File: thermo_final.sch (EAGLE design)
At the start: 109 parts

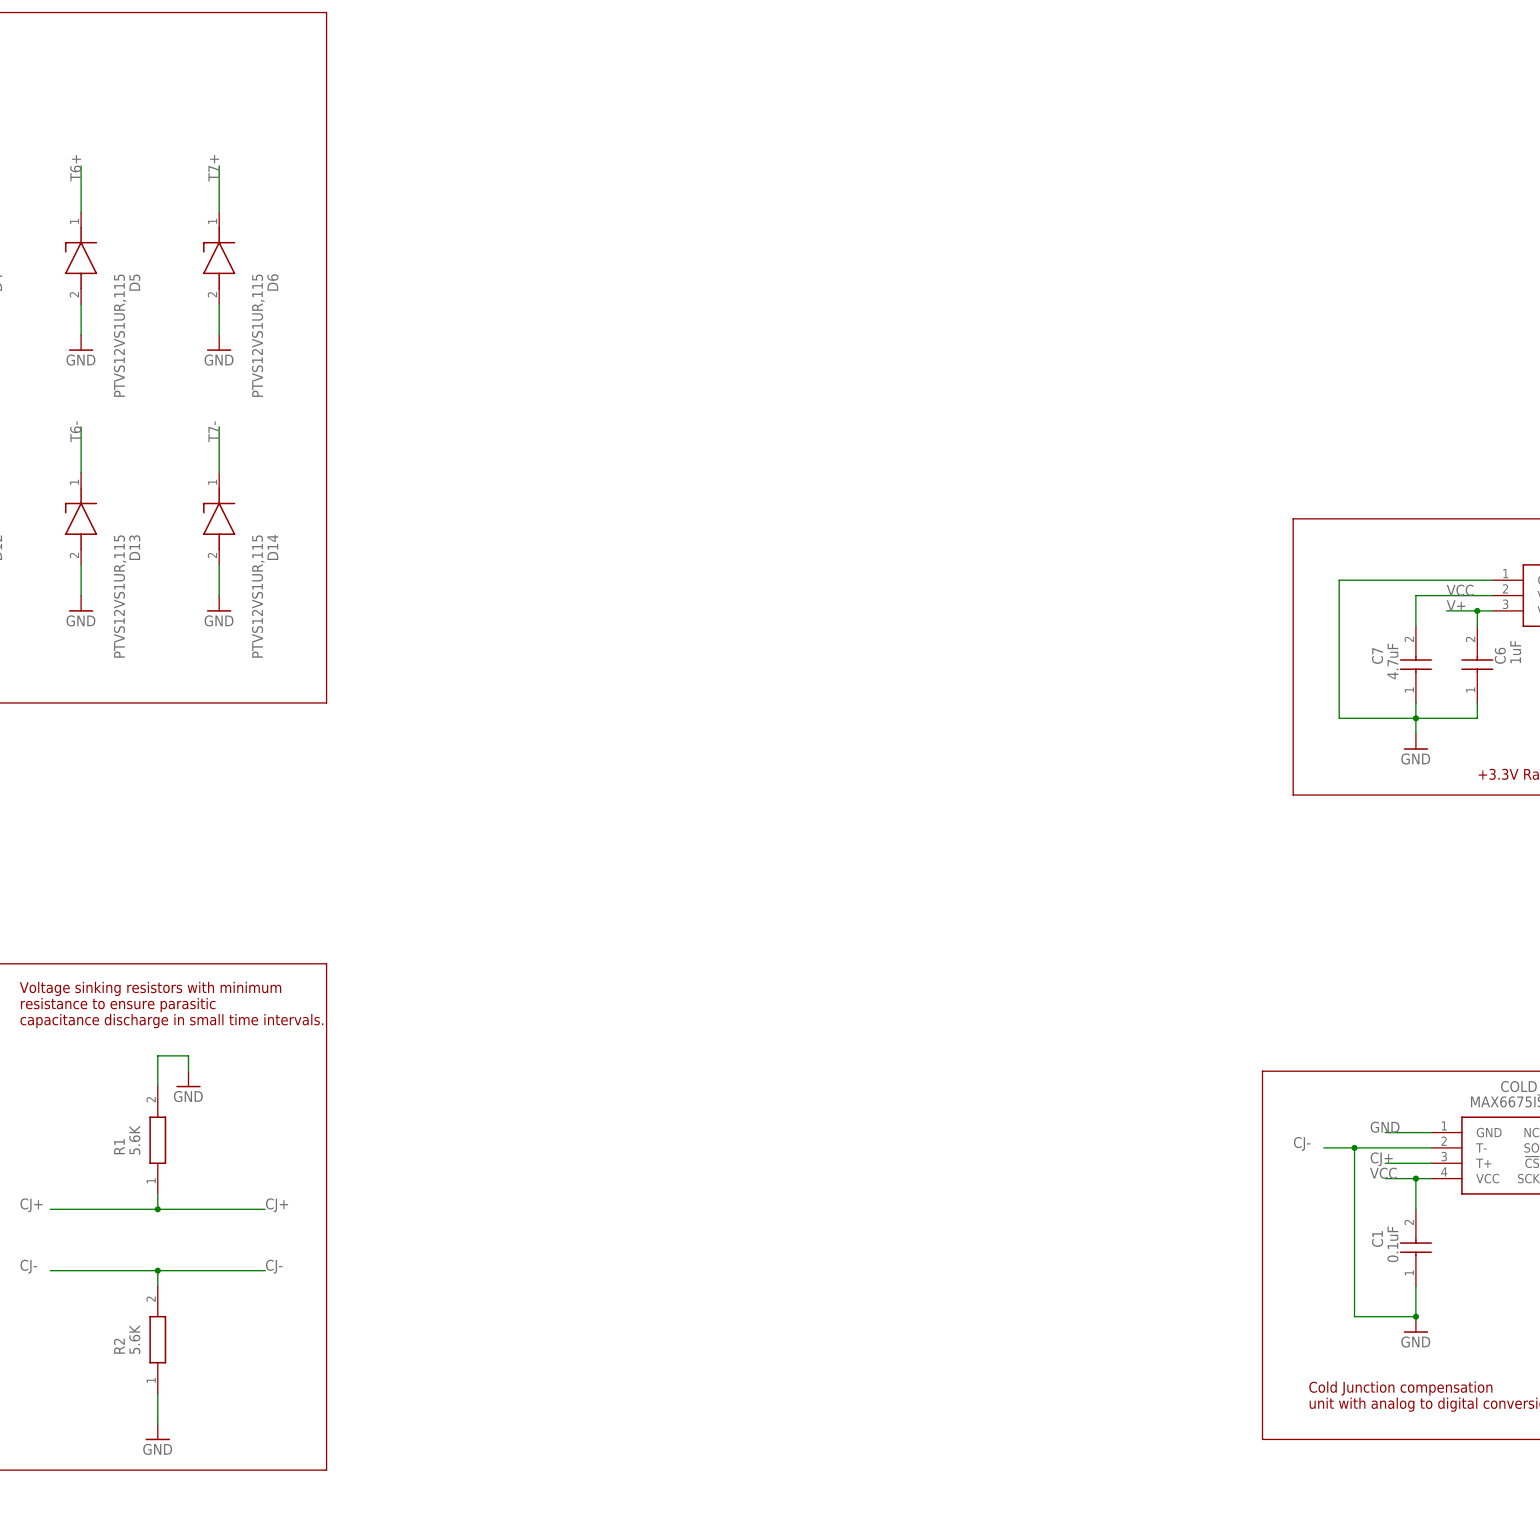
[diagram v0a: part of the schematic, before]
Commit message: Final w/GND vias & Enclosure Holes
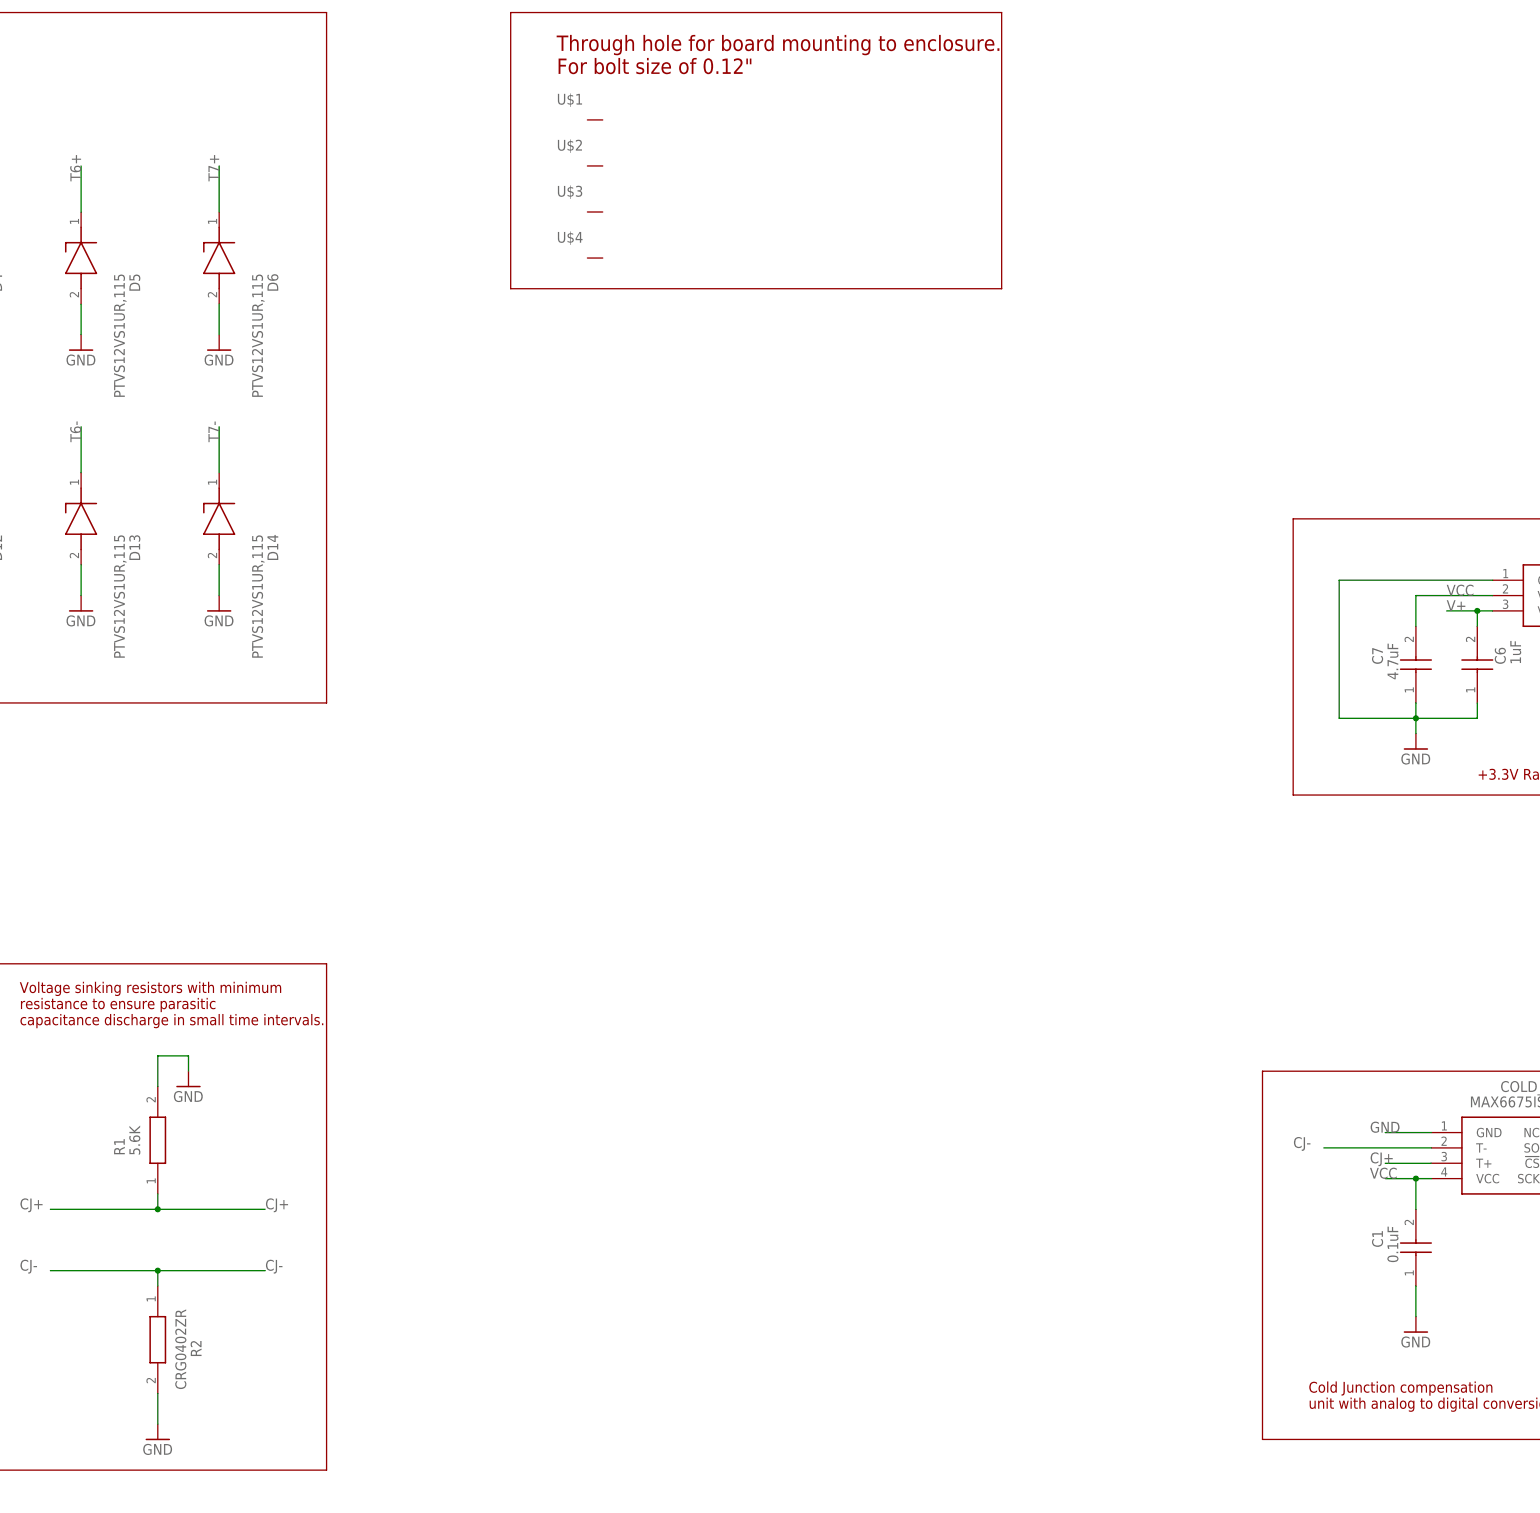
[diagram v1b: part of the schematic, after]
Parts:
- added U$1, U$2, U$3, U$4: THROUGH_HOLE, SamacSys_Parts:THROUGH_HOLE
- R2: value 5.6K -> CRG0402ZR; device SamacSys_Parts:ERA-2ARB562X -> SamacSys_Parts:CRG0402ZR
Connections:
- net CJ-: now also R2.1; no longer C1.1, R2.2
- net GND: now also C1.1, R2.2; no longer R2.1
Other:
- note added: "Through hole for board mounting to enclosure. For bolt size of 0.12""
- moved on the sheet: R2
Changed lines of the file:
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@@
 <part name="GND9" library="supply1" library_urn="urn:adsk.eagle:library:371" deviceset="GND" device=""/>
 <part name="R1" library="SamacSys_Parts" deviceset="ERA-2ARB562X" device="" value="5.6K"/>
-<part name="R2" library="SamacSys_Parts" deviceset="ERA-2ARB562X" device="" value="5.6K"/>
 <part name="GND10" library="supply1" library_urn="urn:adsk.eagle:library:371" deviceset="GND" device=""/>
 <part name="GND11" library="supply1" library_urn="urn:adsk.eagle:library:371" deviceset="GND" device=""/>
@@
 <part name="GND41" library="supply1" library_urn="urn:adsk.eagle:library:371" deviceset="GND" device=""/>
 <part name="GND56" library="supply1" library_urn="urn:adsk.eagle:library:371" deviceset="GND" device=""/>
+<part name="R2" library="SamacSys_Parts" library_urn="urn:adsk.eagle:library:34728992" deviceset="CRG0402ZR" device="" package3d_urn="urn:adsk.eagle:package:34729065/2"/>
+<part name="U$1" library="SamacSys_Parts" library_urn="urn:adsk.eagle:library:34728992" deviceset="THROUGH_HOLE" device=""/>
+<part name="U$2" library="SamacSys_Parts" library_urn="urn:adsk.eagle:library:34728992" deviceset="THROUGH_HOLE" device=""/>
+<part name="U$3" library="SamacSys_Parts" library_urn="urn:adsk.eagle:library:34728992" deviceset="THROUGH_HOLE" device=""/>
+<part name="U$4" library="SamacSys_Parts" library_urn="urn:adsk.eagle:library:34728992" deviceset="THROUGH_HOLE" device=""/>
 </parts>
 <sheets>
@@
 <wire x1="347.98" y1="-38.1" x2="210.82" y2="-38.1" width="0.1524" layer="94"/>
 <text x="294.64" y="-25.4" size="2.54" layer="94">isoSPI (Slave)</text>
+<wire x1="30.48" y1="198.12" x2="30.48" y2="152.4" width="0.1524" layer="94"/>
+<wire x1="30.48" y1="152.4" x2="111.76" y2="152.4" width="0.1524" layer="94"/>
+<wire x1="111.76" y1="152.4" x2="111.76" y2="198.12" width="0.1524" layer="94"/>
+<wire x1="111.76" y1="198.12" x2="30.48" y2="198.12" width="0.1524" layer="94"/>
+<text x="38.1" y="187.96" size="2.54" layer="94">Through hole for board mounting to enclosure.
+For bolt size of 0.12"</text>
 </plain>
 <instances>
@@
 <attribute name="VALUE" x="-31.75" y="8.89" size="1.778" layer="96" rot="R90" align="center-left"/>
 </instance>
-<instance part="R2" gate="G$1" x="-27.94" y="-30.48" smashed="yes" rot="R90">
-<attribute name="NAME" x="-34.29" y="-24.13" size="1.778" layer="95" rot="R90" align="center-left"/>
-<attribute name="VALUE" x="-31.75" y="-24.13" size="1.778" layer="96" rot="R90" align="center-left"/>
-</instance>
 <instance part="GND10" gate="1" x="-22.86" y="20.32" smashed="yes">
 <attribute name="VALUE" x="-25.4" y="17.78" size="1.778" layer="96"/>
@@
 <instance part="GND56" gate="1" x="457.2" y="-22.86" smashed="yes">
 <attribute name="VALUE" x="454.66" y="-25.4" size="1.778" layer="96"/>
+</instance>
+<instance part="R2" gate="G$1" x="-27.94" y="-12.7" smashed="yes" rot="R270">
+<attribute name="NAME" x="-21.59" y="-21.59" size="1.778" layer="95" rot="R270" align="center-left"/>
+<attribute name="VALUE" x="-24.13" y="-16.51" size="1.778" layer="96" rot="R270" align="center-left"/>
+</instance>
+<instance part="U$1" gate="G$1" x="43.18" y="180.34" smashed="yes">
+<attribute name="NAME" x="38.1" y="182.88" size="1.778" layer="95"/>
+</instance>
+<instance part="U$2" gate="G$1" x="43.18" y="172.72" smashed="yes">
+<attribute name="NAME" x="38.1" y="175.26" size="1.778" layer="95"/>
+</instance>
+<instance part="U$3" gate="G$1" x="43.18" y="165.1" smashed="yes">
+<attribute name="NAME" x="38.1" y="167.64" size="1.778" layer="95"/>
+</instance>
+<instance part="U$4" gate="G$1" x="43.18" y="157.48" smashed="yes">
+<attribute name="NAME" x="38.1" y="160.02" size="1.778" layer="95"/>
 </instance>
 </instances>
@@
 </segment>
 <segment>
-<pinref part="C1" gate="G$1" pin="1"/>
-<wire x1="180.34" y1="-12.7" x2="180.34" y2="-17.78" width="0.1524" layer="91"/>
-<pinref part="GND3" gate="1" pin="GND"/>
 <pinref part="COLD_JUNCTION" gate="G$1" pin="T-"/>
-<wire x1="182.88" y1="10.16" x2="170.18" y2="10.16" width="0.1524" layer="91"/>
-<wire x1="170.18" y1="10.16" x2="165.1" y2="10.16" width="0.1524" layer="91"/>
-<wire x1="170.18" y1="10.16" x2="170.18" y2="-17.78" width="0.1524" layer="91"/>
-<wire x1="170.18" y1="-17.78" x2="180.34" y2="-17.78" width="0.1524" layer="91"/>
-<junction x="170.18" y="10.16"/>
-<junction x="180.34" y="-17.78"/>
+<wire x1="182.88" y1="10.16" x2="165.1" y2="10.16" width="0.1524" layer="91"/>
 <label x="160.02" y="10.16" size="1.778" layer="95"/>
 </segment>
 <segment>
-<pinref part="R2" gate="G$1" pin="2"/>
 <wire x1="-27.94" y1="-12.7" x2="-27.94" y2="-10.16" width="0.1524" layer="91"/>
 <wire x1="-27.94" y1="-10.16" x2="-45.72" y2="-10.16" width="0.1524" layer="91"/>
@@
 <label x="-50.8" y="-10.16" size="1.778" layer="95"/>
 <label x="-10.16" y="-10.16" size="1.778" layer="95"/>
+<pinref part="R2" gate="G$1" pin="1"/>
 </segment>
 <segment>
@@
 </segment>
 <segment>
-<pinref part="R2" gate="G$1" pin="1"/>
 <wire x1="-27.94" y1="-30.48" x2="-27.94" y2="-35.56" width="0.1524" layer="91"/>
 <pinref part="GND11" gate="1" pin="GND"/>
+<pinref part="R2" gate="G$1" pin="2"/>
 </segment>
 <segment>
@@
 <pinref part="GND56" gate="1" pin="GND"/>
 </segment>
+<segment>
+<pinref part="C1" gate="G$1" pin="1"/>
+<wire x1="180.34" y1="-12.7" x2="180.34" y2="-17.78" width="0.1524" layer="91"/>
+<pinref part="GND3" gate="1" pin="GND"/>
+</segment>
 </net>

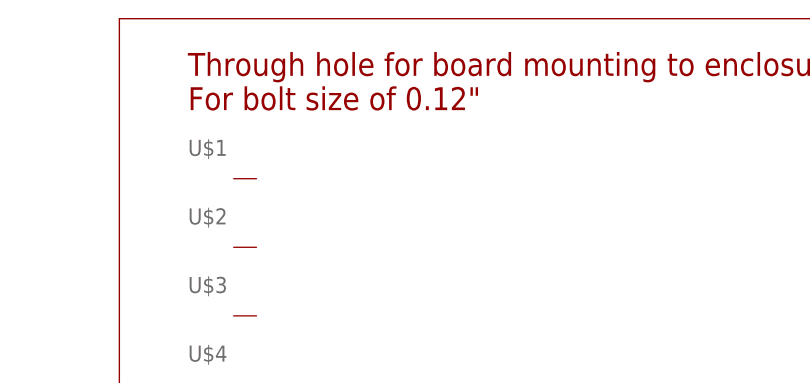
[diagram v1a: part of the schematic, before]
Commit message: Rearranged transformer
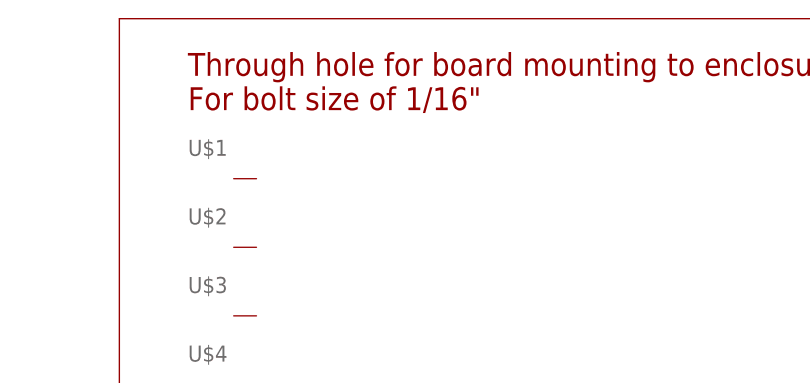
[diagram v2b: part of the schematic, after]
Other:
- note added: "Through hole for board mounting to enclosure. For bolt size of 1/16""
- note removed: "Through hole for board mounting to enclosure. For bolt size of 0.12""
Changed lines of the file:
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@@
 <wire x1="111.76" y1="198.12" x2="30.48" y2="198.12" width="0.1524" layer="94"/>
 <text x="38.1" y="187.96" size="2.54" layer="94">Through hole for board mounting to enclosure.
-For bolt size of 0.12"</text>
+For bolt size of 1/16"</text>
 </plain>
 <instances>

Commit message: Uploaded all necessary 3D models
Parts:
- CONNECTOR_0, CONNECTOR_1, CONNECTOR_2, CONNECTOR_3, CONNECTOR_4, CONNECTOR_5, CONNECTOR_6, CONNECTOR_7: device PCC-SMD-20:PCC-SMD-20 -> SamacSys_Parts:PCC-SMD-20
- R3: device TNPW0402100RBYEP:TNPW0402100RBYEP -> SamacSys_Parts:TNPW0402100RBYEP
